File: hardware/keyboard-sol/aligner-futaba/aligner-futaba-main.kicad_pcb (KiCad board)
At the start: 2 copper layers, 324 x 116.9 mm, 77 parts, among them SW10 TAB: 1.25x, SW11 I, SW12 2, SW13 Zero, SW14 Q, SW15 O, SW16 3, SW17 Dash, SW18 W, SW19 P, SW20 4, SW21 Caret, SW22 E, SW23 AT, SW24 5, SW25 LT Bracket, SW26 R, SW27 Return: 1.5x, SW28 6, SW29 Backslash, SW30 T, SW31 Line Feed, SW32 7, SW33 RT Bracket, SW34 Y, SW35 Load, SW36 LT Ctrl, SW37 J, SW38 Upper Case: 1.5x, SW39 M, SW4 ESC: 1.75x, SW40 Shift Lock: 1.5x, SW41 K, SW42 LT Shift: 1.5x, SW43 Comma, SW44 A, SW45 L, SW46 Z, SW47 Period, SW48 S, SW49 Semicolon, SW5 8, SW50 X, SW51 Slash, SW52 D, SW53 Colon, SW54 C, SW55 RT Shift: 2x, SW56 F, SW57 DEL, SW58 V, SW59 Mode Select: 1.75x, SW6 BREAK, SW60 G, SW61 Repeat: 1.25x, SW62 B, SW63 H, SW64 RT Ctrl, SW65 N, SW66 Local, SW7 U, SW70 Up Arrow, SW74 LT Arrow, SW78 Spacebar, SW8 1, SW81 RT Arrow, SW84 Down Arrow, SW87 Home, SW88 Clear, SW9 9

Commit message: Swapped text in futaba "main" aligner
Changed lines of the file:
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@@
   (gr_circle (center 102.16388 187.74156) (end 105.38968 187.74156) (layer Edge.Cuts) (width 0.12))
   (gr_circle (center 121.21388 168.69156) (end 124.43968 168.69156) (layer Edge.Cuts) (width 0.12))
-  (gr_text "SOL-20 Futaba MD-4PCS aligner (Main) Rev 1.0" (at 307.7464 112.0394) (layer F.SilkS)
+  (gr_text "SOL-20 Futaba MD-4PCS aligner (Main) Rev 1.0" (at 148.1836 112.8268) (layer F.SilkS)
     (effects (font (size 2.032 2.032) (thickness 0.2032)) (justify left))
   )
-  (gr_text "Unified Keyboard Project.   https://github.com/osiweb/unified_retro_keyboard" (at 129.5654 112.4458) (layer F.SilkS)
+  (gr_text "Unified Keyboard Project.   https://github.com/osiweb/unified_retro_keyboard" (at 272.796 112.8268) (layer F.SilkS)
     (effects (font (size 2.032 2.032) (thickness 0.2032)) (justify left))
   )

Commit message: Moved mounting slots from keyboard PCB to aligners
- This allows the PCB to sink below the mounting brackets.  The aligner height can
be adjusted relative to the mounting brackets using spacers.

- changed futaba aligners to use cherry stabilizers.

- bumped rev number
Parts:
- removed the REF** at (318.1, 206.8)
- removed the REF** at (184.8, 206.8)
- SW55: footprint unikbd:Futaba-MD-4PCS-aligner -> unikbd:Futaba_2u_Cherry_aligner
- SW78: footprint unikbd:Futaba-MD-4PCS-aligner -> unikbd:Futaba_space_Cherry_aligner
- moved REF** 5.95 mm to (256.2, 114.1)
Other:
- board size 324 x 116.9 mm -> 342.4 x 117.7 mm
- board text added: "SOL-20 Futabe MD-4PCS aligner (main) Rev 1.1"
- board text removed: "SOL-20 Futaba MD-4PCS aligner (Main) Rev 1.0"

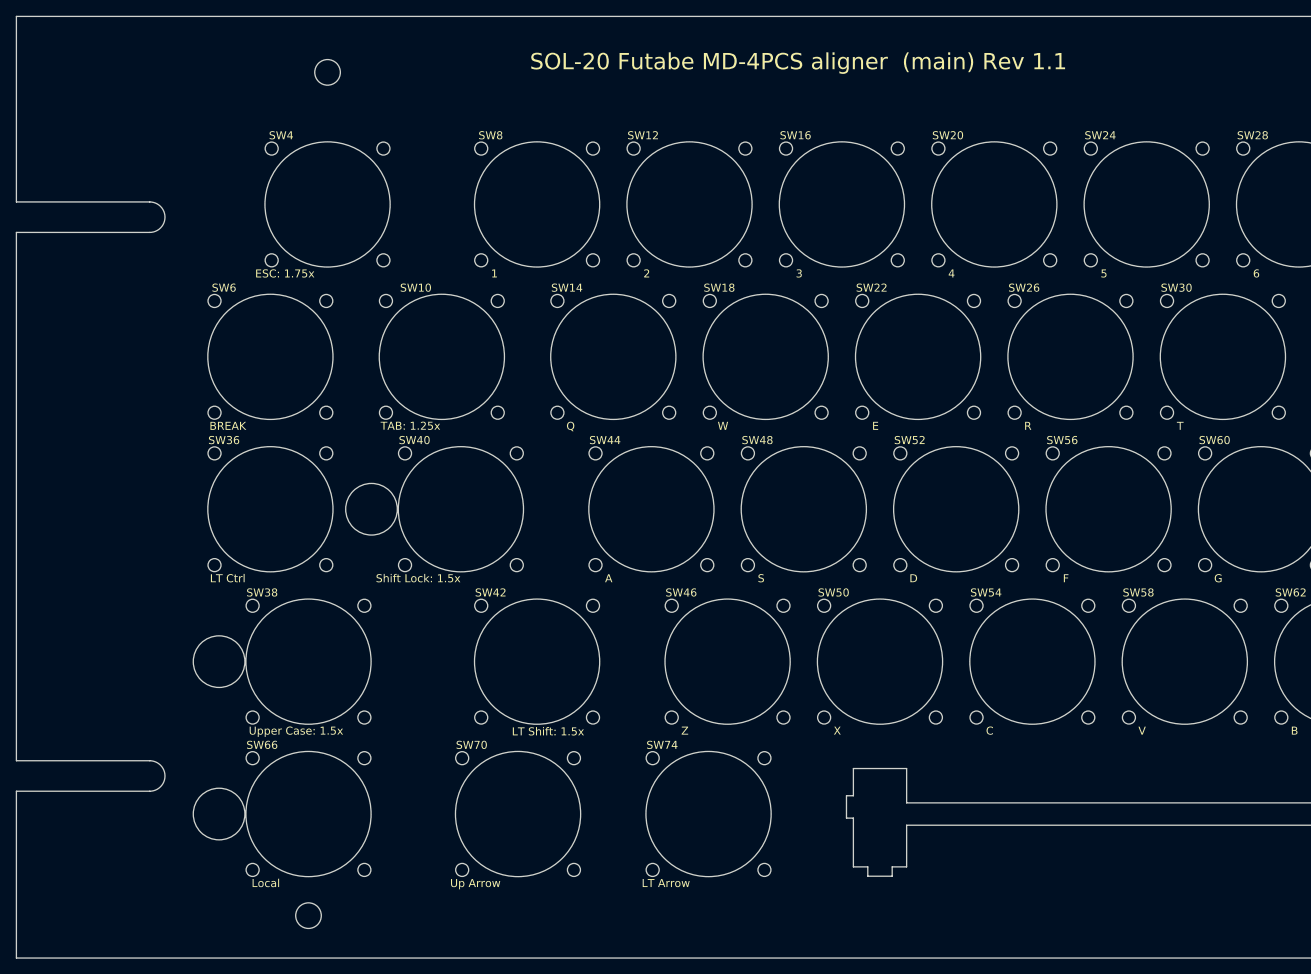
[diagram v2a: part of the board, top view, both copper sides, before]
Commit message: Adjsut mounting slots and alignment of mounting holes.
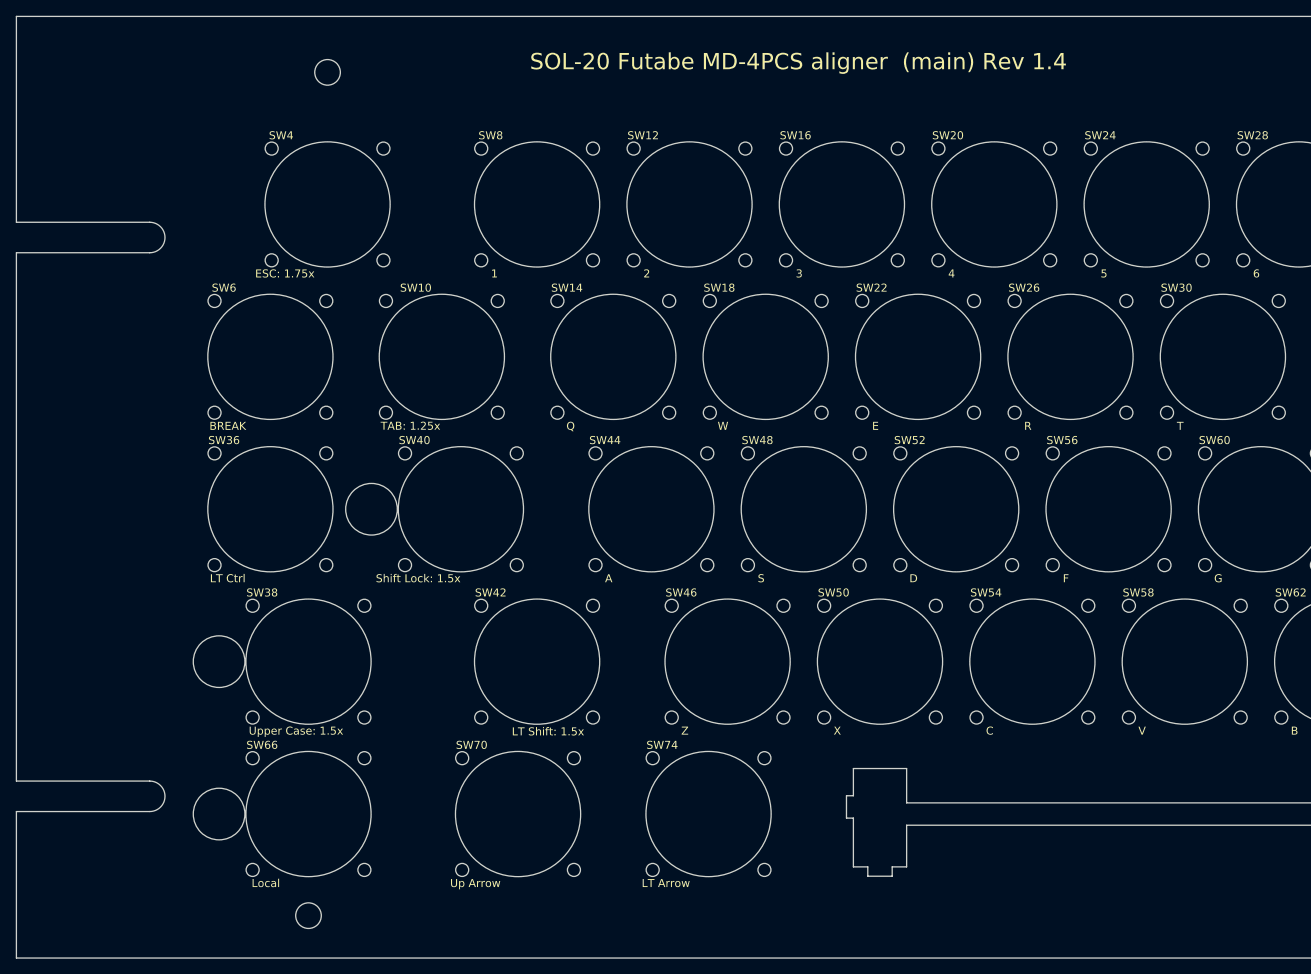
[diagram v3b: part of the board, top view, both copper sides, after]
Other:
- outline, holes or cut-outs redrawn
- board text added: "SOL-20 Futabe MD-4PCS aligner (main) Rev 1.4"
- board text removed: "SOL-20 Futabe MD-4PCS aligner (main) Rev 1.1"
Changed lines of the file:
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@@
   (gr_circle (center 102.16388 187.74156) (end 105.38968 187.74156) (layer Edge.Cuts) (width 0.12))
   (gr_circle (center 121.21388 168.69156) (end 124.43968 168.69156) (layer Edge.Cuts) (width 0.12))
-  (gr_text "SOL-20 Futabe MD-4PCS aligner  (main) Rev 1.1\n" (at 140.9954 112.7506) (layer F.SilkS)
+  (gr_text "SOL-20 Futabe MD-4PCS aligner  (main) Rev 1.4\n" (at 140.9954 112.7506) (layer F.SilkS)
     (effects (font (size 2.032 2.032) (thickness 0.2032)) (justify left))
   )
@@
     (effects (font (size 2.032 2.032) (thickness 0.3048)) (justify left))
   )
-  (gr_line (start 76.82738 134.08914) (end 76.82738 200.12914) (layer Edge.Cuts) (width 0.1016))
-  (gr_line (start 76.82738 107.0864) (end 76.82738 130.27914) (layer Edge.Cuts) (width 0.1016))
-  (gr_line (start 93.49613 130.27914) (end 76.82738 130.27914) (layer Edge.Cuts) (width 0.1016))
-  (gr_line (start 93.49613 134.08914) (end 76.82738 134.08914) (layer Edge.Cuts) (width 0.1016))
-  (gr_arc (start 93.49613 132.18414) (end 93.49613 130.27914) (angle 180) (layer Edge.Cuts) (width 0.1016))
-  (gr_line (start 93.49613 203.93914) (end 76.82738 203.93914) (layer Edge.Cuts) (width 0.1016))
-  (gr_line (start 93.49613 200.12914) (end 76.82738 200.12914) (layer Edge.Cuts) (width 0.1016))
-  (gr_line (start 76.82738 224.79) (end 76.82738 203.93914) (layer Edge.Cuts) (width 0.1016))
-  (gr_arc (start 93.49613 202.03414) (end 93.49613 200.12914) (angle 180) (layer Edge.Cuts) (width 0.1016))
+  (gr_line (start 76.82738 136.62914) (end 76.82738 202.66914) (layer Edge.Cuts) (width 0.1016))
+  (gr_line (start 76.82738 107.0864) (end 76.82738 132.81914) (layer Edge.Cuts) (width 0.1016))
+  (gr_line (start 93.49613 132.81914) (end 76.82738 132.81914) (layer Edge.Cuts) (width 0.1016))
+  (gr_line (start 93.49613 136.62914) (end 76.82738 136.62914) (layer Edge.Cuts) (width 0.1016))
+  (gr_arc (start 93.49613 134.72414) (end 93.49613 132.81914) (angle 180) (layer Edge.Cuts) (width 0.1016))
+  (gr_line (start 93.49613 206.47914) (end 76.82738 206.47914) (layer Edge.Cuts) (width 0.1016))
+  (gr_line (start 93.49613 202.66914) (end 76.82738 202.66914) (layer Edge.Cuts) (width 0.1016))
+  (gr_line (start 76.82738 224.79) (end 76.82738 206.47914) (layer Edge.Cuts) (width 0.1016))
+  (gr_arc (start 93.49613 204.57414) (end 93.49613 202.66914) (angle 180) (layer Edge.Cuts) (width 0.1016))
   (gr_line (start 76.82738 224.79) (end 419.227 224.79) (layer Edge.Cuts) (width 0.1))
   (gr_line (start 419.227 107.0864) (end 76.82738 107.0864) (layer Edge.Cuts) (width 0.1016))
